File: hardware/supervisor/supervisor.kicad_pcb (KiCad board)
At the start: 2 copper layers, 65 x 56.5 mm, 149 parts, among them IC1 ULN2003A, IC2 LM2596-3.3, IC3 MAX11612, IC4 ACS723LLCTR-10AU-T, IC5 ACS723LLCTR-10AU-T, IC6 ACS723LLCTR-10AU-T, IC7 NLSX4373, IC8 NLSX4373, IC9 SIM900, K1 PRINTRELAY_SERIE_36, K2 PRINTRELAY_SERIE_36, P1 CONN_01X02, P2 RASPI-CONNECT, P3 POWER, P4 RELAY CONNECTOR, P5 CONN_01X02, P6 string0, P7 string1, P8 string2, P9 CONN_01X02, SW1 SW_PUSH, SW2 SW_PUSH, U1 SC16IS740IPW, U10 CD74HC4046, U11 CD74HC4046, U12 OPA376AIDCK, U13 CD74HC4046, U14 CD74HC4046, U2 SC16IS740IPW, U3 SC16IS740IPW, U4 RF_CONN, U5 SIM_HOLDER, U6 OPA376AIDCK, U7 CD74HC4046, U8 CD74HC4046, U9 OPA376AIDCK

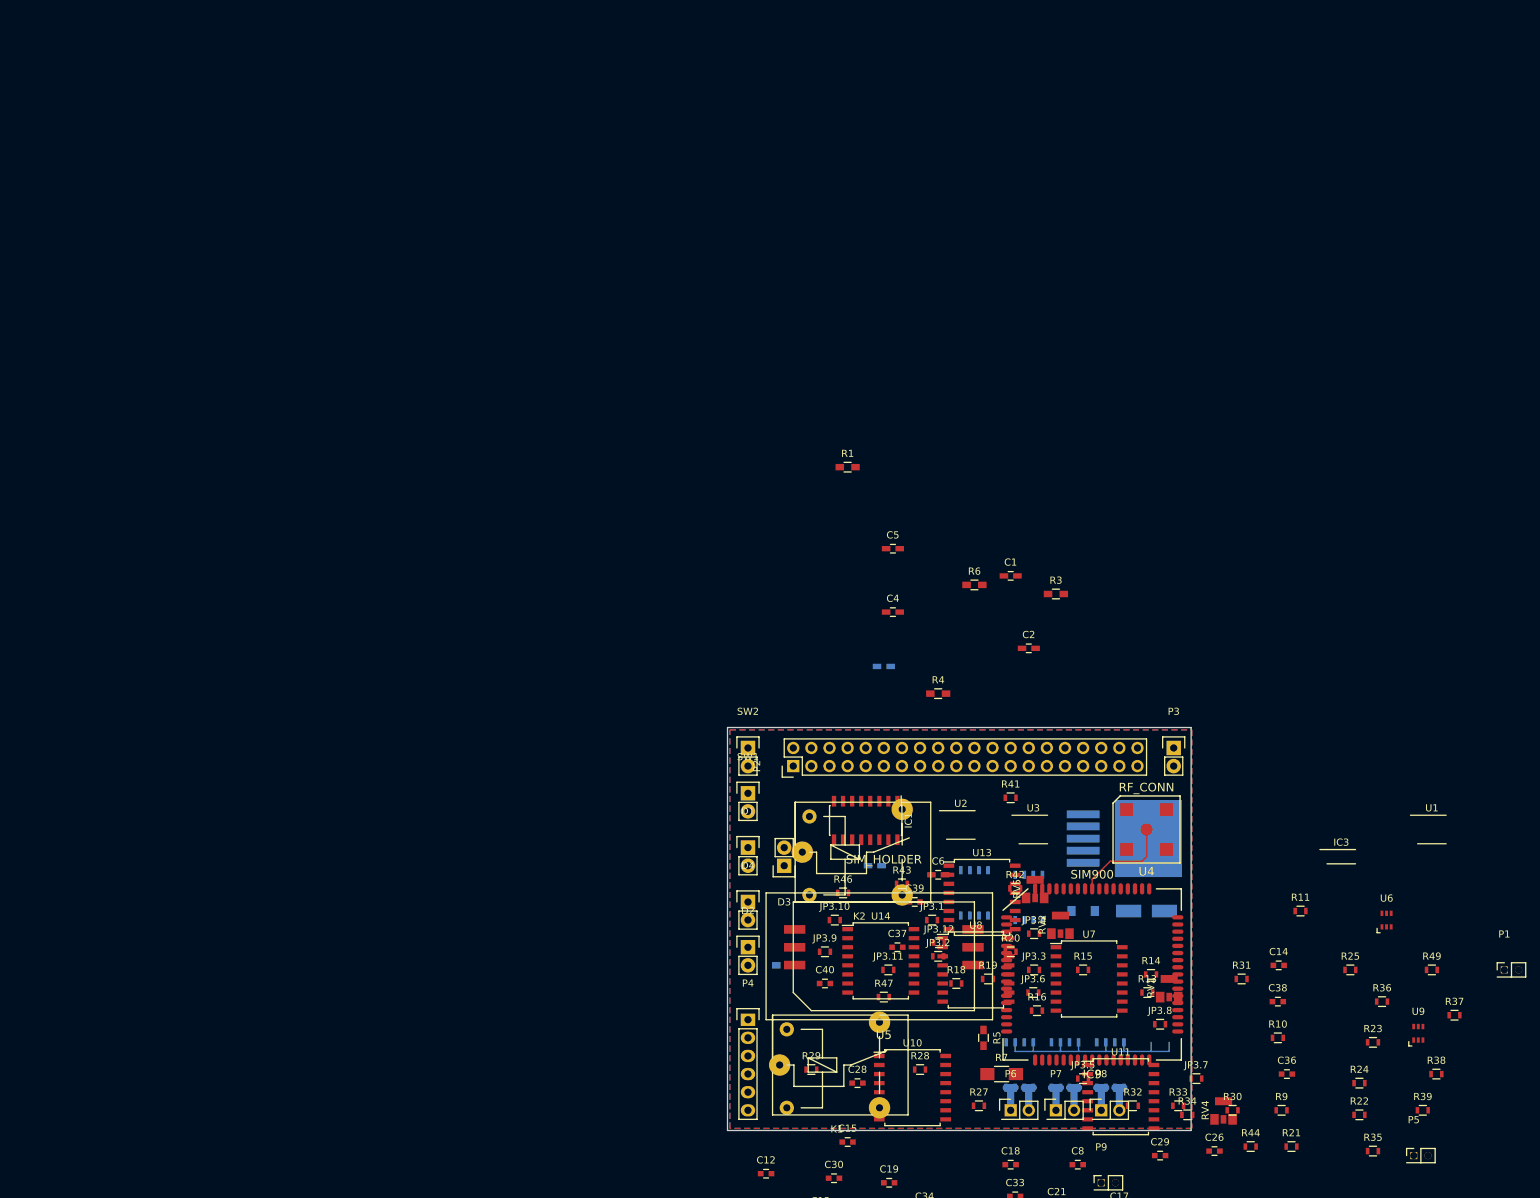
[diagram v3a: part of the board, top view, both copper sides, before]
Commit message: create pcb outline for master
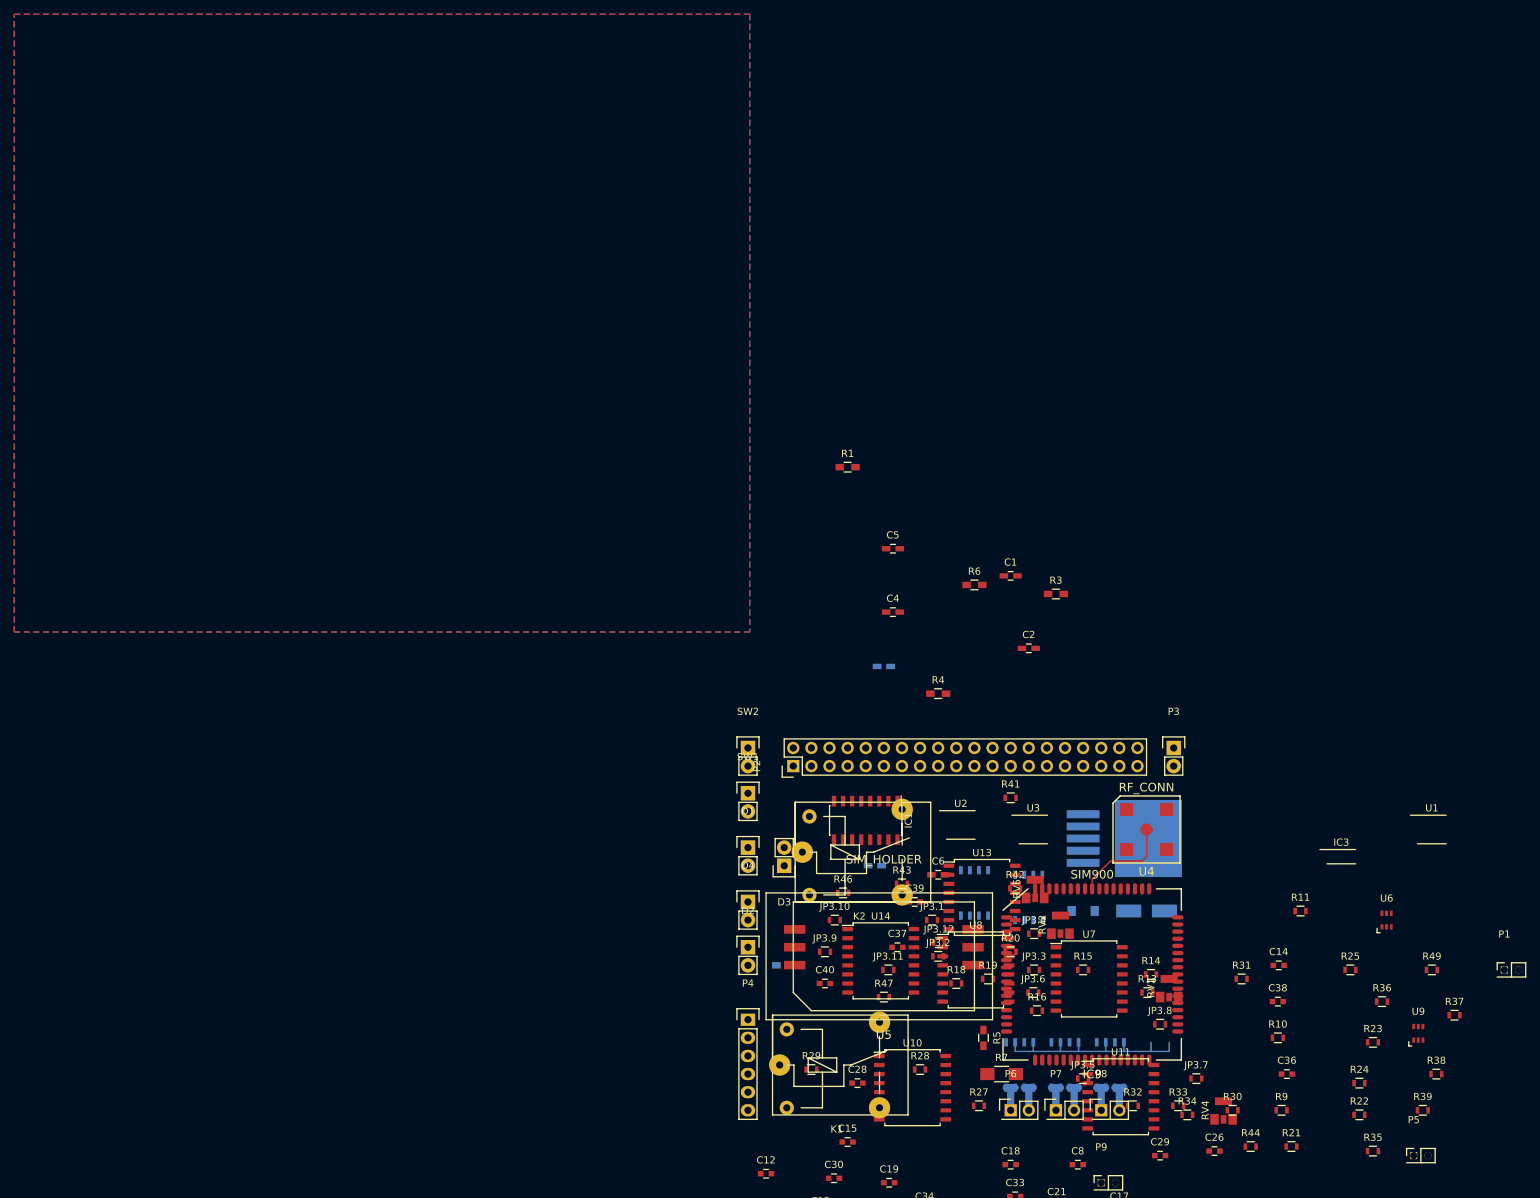
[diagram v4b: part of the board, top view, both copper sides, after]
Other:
- board outline removed
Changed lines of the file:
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@@
-(kicad_pcb (version 4) (host pcbnew 4.0.2-stable)
+(kicad_pcb (version 4) (host pcbnew 4.0.2+dfsg1-stable)
   (general
     (links 389)
-    (no_connects 285)
-    (area 99.999499 99.999499 165.000501 156.500501)
+    (no_connects 325)
+    (area 94.77119 59.675 214.823334 195.831)
     (thickness 1.6)
-    (drawings 4)
+    (drawings 0)
     (tracks 36)
     (zones 0)
@@
     (pad_drill 0.762)
     (pad_to_mask_clearance 0.2)
-    (aux_axis_origin 99.06 99.06)
-    (grid_origin 99.06 99.06)
-    (visible_elements 7FFFEFFF)
+    (aux_axis_origin 0 0)
+    (visible_elements 7FFFE7FF)
     (pcbplotparams
       (layerselection 0x00030_80000001)
@@
     (attr smd)
     (fp_text reference IC3 (at 0 -2) (layer F.SilkS)
-      (effects (font (size 1 1)))
+      (effects (font (size 1 1) (thickness 0.15)))
     )
     (fp_text value MAX11612 (at 0 2) (layer F.Fab)
-      (effects (font (size 1 1)))
+      (effects (font (size 1 1) (thickness 0.15)))
     )
     (fp_line (start -3 -1) (end -3 1) (layer F.CrtYd) (width 0))
@@
     (descr "relay, Sanyou SRD series Form C")
     (fp_text reference K1 (at 8 9) (layer F.SilkS)
-      (effects (font (size 1 1)))
+      (effects (font (size 1 1) (thickness 0.15)))
     )
     (fp_text value PRINTRELAY_SERIE_36 (at 8 -9) (layer F.Fab)
-      (effects (font (size 1 1)))
+      (effects (font (size 1 1) (thickness 0.15)))
     )
     (fp_line (start 15 7) (end 18 7) (layer F.SilkS) (width 0))
@@
     (descr "relay, Sanyou SRD series Form C")
     (fp_text reference K2 (at 8 9) (layer F.SilkS)
-      (effects (font (size 1 1)))
+      (effects (font (size 1 1) (thickness 0.15)))
     )
     (fp_text value PRINTRELAY_SERIE_36 (at 8 -9) (layer F.Fab)
-      (effects (font (size 1 1)))
+      (effects (font (size 1 1) (thickness 0.15)))
     )
     (fp_line (start 15 7) (end 18 7) (layer F.SilkS) (width 0))
@@
     (tags "pin header")
     (fp_text reference P1 (at 0 -5) (layer F.SilkS)
-      (effects (font (size 1 1)))
+      (effects (font (size 1 1) (thickness 0.15)))
     )
     (fp_text value CONN_01X02 (at 0 -3) (layer F.Fab)
-      (effects (font (size 1 1)))
+      (effects (font (size 1 1) (thickness 0.15)))
     )
     (fp_line (start -1 -1) (end -1 1) (layer F.CrtYd) (width 0))
@@
     (tags "pin header")
     (fp_text reference P5 (at 0 -5) (layer F.SilkS)
-      (effects (font (size 1 1)))
+      (effects (font (size 1 1) (thickness 0.15)))
     )
     (fp_text value CONN_01X02 (at 0 -3) (layer F.Fab)
-      (effects (font (size 1 1)))
+      (effects (font (size 1 1) (thickness 0.15)))
     )
     (fp_line (start -1 -1) (end -1 1) (layer F.CrtYd) (width 0))
@@
     (tags "pin header")
     (fp_text reference P9 (at 0 -5) (layer F.SilkS)
-      (effects (font (size 1 1)))
+      (effects (font (size 1 1) (thickness 0.15)))
     )
     (fp_text value CONN_01X02 (at 0 -3) (layer F.Fab)
-      (effects (font (size 1 1)))
+      (effects (font (size 1 1) (thickness 0.15)))
     )
     (fp_line (start -1 -1) (end -1 1) (layer F.CrtYd) (width 0))
@@
     (attr smd)
     (fp_text reference U1 (at 0 -3) (layer F.SilkS)
-      (effects (font (size 1 1)))
+      (effects (font (size 1 1) (thickness 0.15)))
     )
     (fp_text value SC16IS740IPW (at 0 3) (layer F.Fab)
-      (effects (font (size 1 1)))
+      (effects (font (size 1 1) (thickness 0.15)))
     )
     (fp_line (start -3 -2) (end -3 2) (layer F.CrtYd) (width 0))
@@
     (attr smd)
     (fp_text reference U2 (at 0 -3) (layer F.SilkS)
-      (effects (font (size 1 1)))
+      (effects (font (size 1 1) (thickness 0.15)))
     )
     (fp_text value SC16IS740IPW (at 0 3) (layer F.Fab)
-      (effects (font (size 1 1)))
+      (effects (font (size 1 1) (thickness 0.15)))
     )
     (fp_line (start -3 -2) (end -3 2) (layer F.CrtYd) (width 0))
@@
     (attr smd)
     (fp_text reference U3 (at 0 -3) (layer F.SilkS)
-      (effects (font (size 1 1)))
+      (effects (font (size 1 1) (thickness 0.15)))
     )
     (fp_text value SC16IS740IPW (at 0 3) (layer F.Fab)
-      (effects (font (size 1 1)))
+      (effects (font (size 1 1) (thickness 0.15)))
     )
     (fp_line (start -3 -2) (end -3 2) (layer F.CrtYd) (width 0))
@@
     )
   )
-  (gr_line (start 100 156.5) (end 100 100) (angle 90) (layer Edge.Cuts) (width 0.001))
-  (gr_line (start 165 156.5) (end 100 156.5) (angle 90) (layer Edge.Cuts) (width 0.001))
-  (gr_line (start 165 100) (end 165 156.5) (angle 90) (layer Edge.Cuts) (width 0.001))
-  (gr_line (start 100 100) (end 165 100) (angle 90) (layer Edge.Cuts) (width 0.001))
   (segment (start 142.875 145.415) (end 146.685 145.415) (width 0.2) (layer B.Cu) (net 1))
   (segment (start 146.685 144.145) (end 146.685 145.415) (width 0.2) (layer B.Cu) (net 1))
@@
     (polygon
       (pts
-        (xy 165.1 156.21) (xy 100.33 156.21) (xy 100.33 100.33) (xy 165.1 100.33) (xy 165.1 156.21)
+        (xy 103.124 86.614) (xy 0 86.614) (xy 0 0) (xy 103.124 0)
       )
     )
@@
     (polygon
       (pts
-        (xy 165.1 156.21) (xy 100.33 156.21) (xy 100.33 100.33) (xy 165.1 100.33) (xy 165.1 156.21)
+        (xy 103.124 0) (xy 103.124 86.614) (xy 0 86.614) (xy 0 0)
       )
     )

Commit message: restart layouting
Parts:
- D5, IC2, IC4, IC5, IC6, IC7, IC8, L1: moved to F.Cu
- moved U1 171.7 mm to (43.4, 41.1)
- moved P3 150.6 mm to (46.5, 6.86)
- moved U7 147.5 mm to (15.5, 76.2)
- moved D1 131.8 mm to (10.2, 23.1)
- moved D2 131.8 mm to (10.2, 37.1)
- moved D4 131.8 mm to (10.2, 30.7)
- moved SW1 131.8 mm to (10.2, 15.5)
- moved SW2 131.8 mm to (10.2, 9.14)
- moved U11 130.7 mm to (60.5, 61.7)
- moved P4 129.2 mm to (6.35, 55.1)
- moved IC1 128.8 mm to (37.3, 13.7)
- moved IC2 128.7 mm to (63.2, 20.3), turned to 270 degrees
- moved K1 128.3 mm to (16.3, 56.9)
- moved IC9 128.2 mm to (86.1, 24.1)
- moved K2 125.8 mm to (17.5, 32.8)
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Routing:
- net +5V: track 31.7 -> 0.00 mm
- net Net-(IC9-Pad60): track 14.1 -> 0.00 mm
- net string_out2: track 4.44 -> 0.00 mm
- net string_out1: track 4.44 -> 0.00 mm
- net string_out0: track 4.44 -> 0.00 mm
- net string_in0: track 4.44 -> 0.00 mm
- net string_in2: track 4.44 -> 0.00 mm
- net string_in1: track 4.44 -> 0.00 mm

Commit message: fix/rollback
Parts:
- K1, K2: value PRINTRELAY_SERIE_36 -> RELAY_SERIE_36; footprint Relays_ThroughHole:Relay_SANYOU_SRD_Series_Form_C -> pro4:RELAY_SERIE_36
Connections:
- C19 pad 1: /FSK Module/coupling -> /FSK Module 2/coupling2
- C30 pad 1: /FSK Module/coupling -> /FSK Module 3/coupling3
- C8 pad 1: /FSK Module/coupling -> /FSK Module 1/coupling1
- IC1 pad 11: (no net) -> Net-(IC1-Pad11)
- IC1 pad 12: (no net) -> Net-(IC1-Pad12)
- JP3.1 pad 2: /FSK Module/JP2 -> /FSK Module 1/JP1
- JP3.10 pad 2: /FSK Module/VCOin -> /FSK Module 3/VCO3in
- JP3.11 pad 1: /FSK Module/VCOin -> /FSK Module 3/VCO3in
- JP3.12 pad 1: /FSK Module/VCOin -> /FSK Module 3/VCO3in
- JP3.2 pad 2: /FSK Module/VCOin -> /FSK Module 1/VCOin1
- JP3.3 pad 1: /FSK Module/VCOin -> /FSK Module 1/VCOin1
- JP3.4 pad 1: /FSK Module/VCOin -> /FSK Module 1/VCOin1
- JP3.5 pad 2: /FSK Module/JP2 -> /FSK Module 2/JP2
- JP3.6 pad 2: /FSK Module/VCOin -> /FSK Module 2/VCOin2
- JP3.7 pad 1: /FSK Module/VCOin -> /FSK Module 2/VCOin2
- JP3.8 pad 1: /FSK Module/VCOin -> /FSK Module 2/VCOin2
- JP3.9 pad 2: /FSK Module/JP2 -> /FSK Module 3/JP3
- P1 pad 2: /FSK Module/coupling -> /FSK Module 1/coupling1
- P4 pad 1: Net-(K1-Pad1) -> Net-(K1-Pad14)
- P4 pad 2: Net-(K1-Pad5) -> Net-(K1-Pad11)
- P4 pad 3: Net-(K1-Pad3) -> Net-(K1-Pad12)
- P4 pad 4: Net-(K2-Pad1) -> Net-(K2-Pad14)
- P4 pad 5: Net-(K2-Pad5) -> Net-(K2-Pad11)
- P4 pad 6: Net-(K2-Pad3) -> Net-(K2-Pad12)
- P5 pad 2: /FSK Module/coupling -> /FSK Module 2/coupling2
- P9 pad 2: /FSK Module/coupling -> /FSK Module 3/coupling3
- R10 pad 2: /FSK Module/coupling -> /FSK Module 1/coupling1
- R11 pad 1: /FSK Module/coupling -> /FSK Module 1/coupling1
- R16 pad 1: /FSK Module/VCOin -> /FSK Module 1/VCOin1
- R21 pad 2: /FSK Module/incoming -> /FSK Module 1/incoming1
- R22 pad 2: /FSK Module/outgoing -> (no net)
- R24 pad 2: /FSK Module/coupling -> /FSK Module 2/coupling2
- R25 pad 1: /FSK Module/coupling -> /FSK Module 2/coupling2
- R30 pad 1: /FSK Module/VCOin -> /FSK Module 2/VCOin2
- R35 pad 2: /FSK Module/incoming -> /FSK Module 2/RX2_out
- R36 pad 2: /FSK Module/outgoing -> /FSK Module 3/outgoing3
- R38 pad 2: /FSK Module/coupling -> /FSK Module 3/coupling3
- R39 pad 1: /FSK Module/coupling -> /FSK Module 3/coupling3
- R44 pad 1: /FSK Module/VCOin -> /FSK Module 3/VCO3in
- R49 pad 2: /FSK Module/incoming -> /FSK Module 3/incoming3
- R8 pad 2: /FSK Module/outgoing -> /FSK Module 1/outgoing1
- U1 pad 12: /FSK Module/outgoing -> /FSK Module 1/outgoing1
- U1 pad 13: /FSK Module/incoming -> /FSK Module 1/incoming1
- U10 pad 4: /FSK Module/coupling -> /FSK Module 2/coupling2
- U11 pad 10: /FSK Module/incoming -> /FSK Module 2/RX2_out
- U11 pad 3: /FSK Module/JP2 -> /FSK Module 2/JP2
- U12 pad 1: /FSK Module/coupling -> /FSK Module 3/coupling3
- U13 pad 4: /FSK Module/coupling -> /FSK Module 3/coupling3
- U14 pad 10: /FSK Module/incoming -> /FSK Module 3/incoming3
- U14 pad 3: /FSK Module/JP2 -> /FSK Module 3/JP3
- U2 pad 12: /FSK Module/outgoing -> (no net)
- U2 pad 13: /FSK Module/incoming -> (no net)
- U3 pad 12: /FSK Module/outgoing -> /FSK Module 3/outgoing3
- U3 pad 13: /FSK Module/incoming -> /FSK Module 3/incoming3
- U6 pad 1: /FSK Module/coupling -> /FSK Module 1/coupling1
- U7 pad 4: /FSK Module/coupling -> /FSK Module 1/coupling1
- U8 pad 10: /FSK Module/incoming -> /FSK Module 1/incoming1
- U8 pad 3: /FSK Module/JP2 -> /FSK Module 1/JP1
- U9 pad 1: /FSK Module/coupling -> /FSK Module 2/coupling2

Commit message: swap adc package
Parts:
- C3, C7, R2: moved to F.Cu
- IC3: footprint Housings_SSOP:TSSOP-8_4.4x3mm_Pitch0.65mm -> Housings_SSOP:MSOP-8_3x3mm_Pitch0.65mm
- moved IC3 18.5 mm to (93.3, 99.1)

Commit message: ordered master footprints
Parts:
- moved C13 278.0 mm to (276.2, 193.0)
- moved C12 274.9 mm to (276.2, 195.6), turned to 180 degrees
- moved C3 274.2 mm to (267.3, 193.0)
- moved C22 270.5 mm to (276.2, 179.7), turned to 180 degrees
- moved C27 269.1 mm to (276.4, 173.0), turned to 180 degrees
- moved C11 266.6 mm to (276.3, 175.9), turned to 180 degrees
- moved C34 263.2 mm to (276.2, 190.5), turned to 180 degrees
- moved C24 260.7 mm to (276.2, 183.3)
- moved C16 255.4 mm to (276.4, 170.9), turned to 180 degrees
- moved C33 250.6 mm to (276.3, 187.3), turned to 180 degrees
- moved C35 249.5 mm to (276.4, 168.7)
- moved C15 228.9 mm to (232.4, 169.5)
- moved R47 226.9 mm to (236.7, 137.4)
- moved C38 224.9 mm to (276.2, 198.8), turned to 180 degrees
- moved JP3.11 221.8 mm to (232.4, 132.1), turned to 180 degrees
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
